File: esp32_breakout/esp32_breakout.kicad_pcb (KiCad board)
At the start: 2 copper layers, 48.3 x 70.4 mm, 16 parts, among them J10 UART1, J12 SPI1, J14 DAC1, J15 DAC2, J16 SPI2, U1 ESP32-DEVKITC-32D, X1 AUX1, X2 AUX2

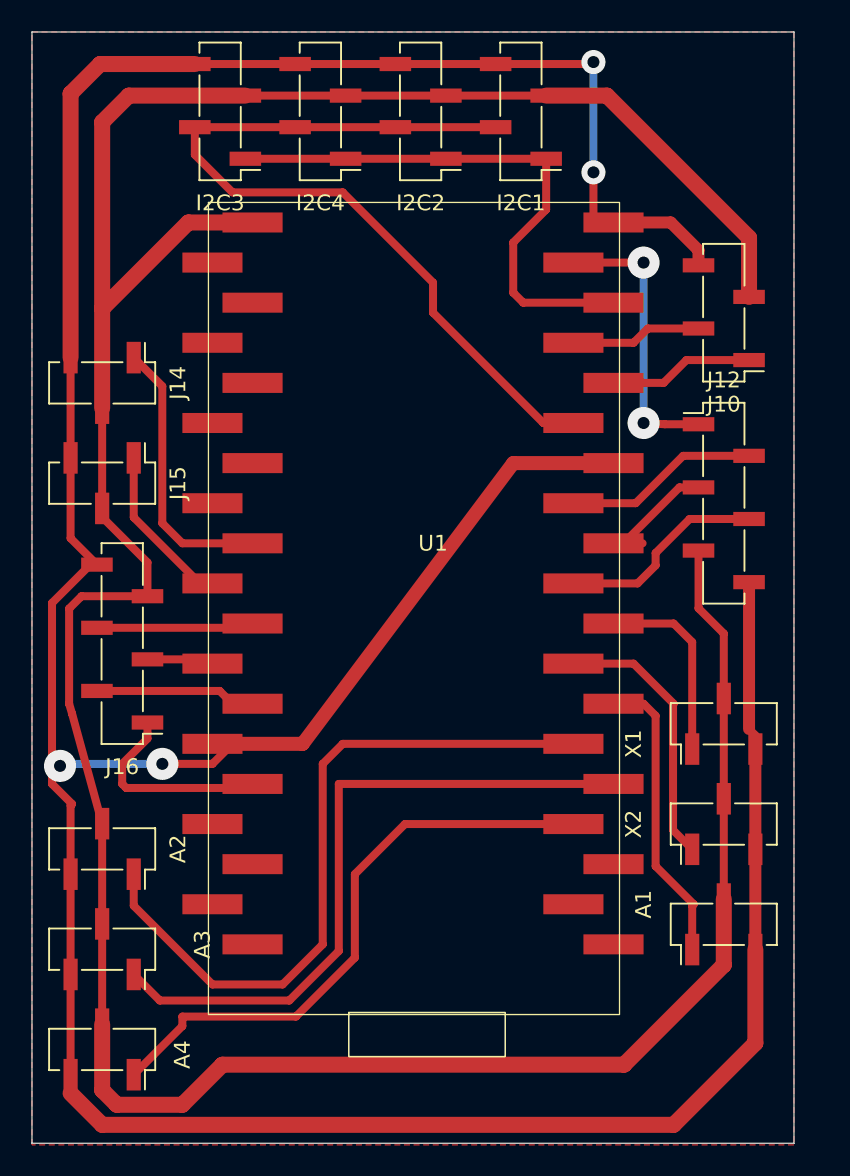
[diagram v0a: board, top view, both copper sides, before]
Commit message: little bigger board
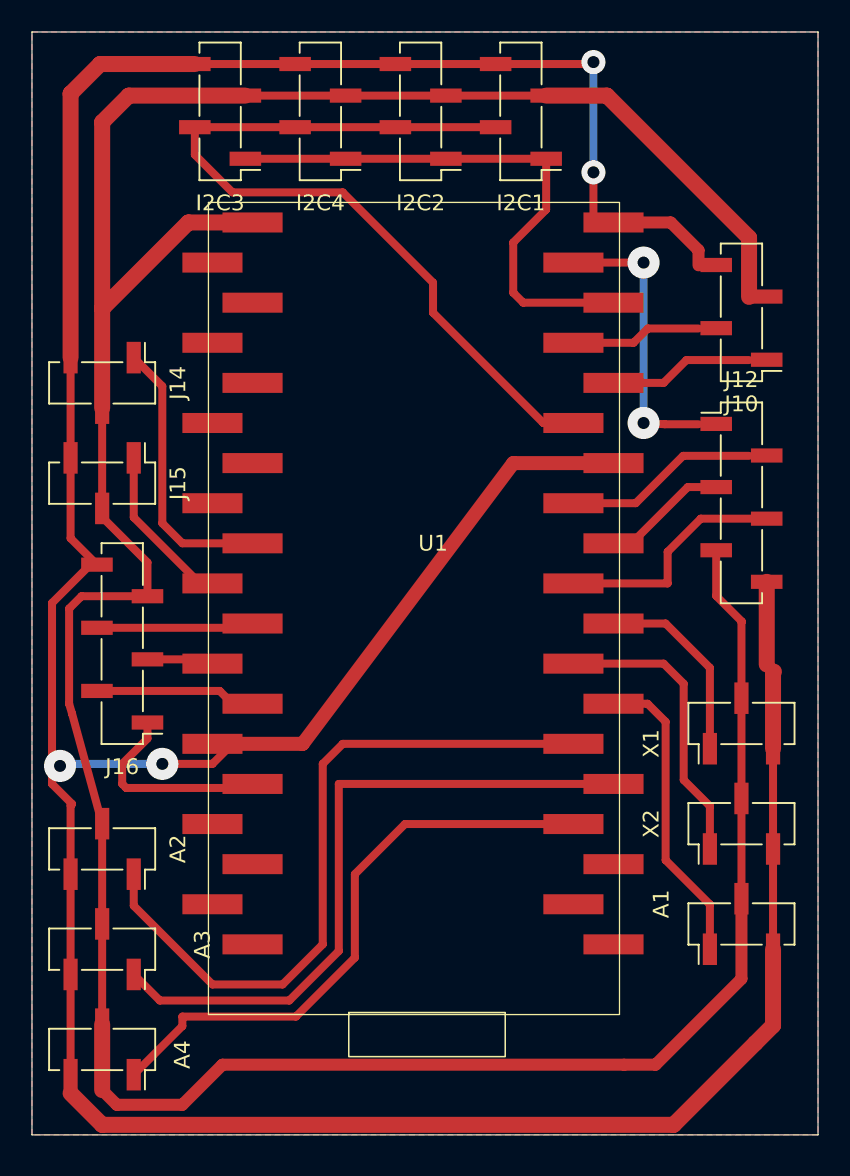
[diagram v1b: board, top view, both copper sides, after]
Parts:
- moved A1 1.12 mm to (44.9, 56.5)
- moved J10 1.12 mm to (44.9, 17.8)
- moved J12 1.12 mm to (44.9, 29.8)
- moved X1 1.12 mm to (44.9, 43.8)
- moved X2 1.12 mm to (44.9, 50.1)
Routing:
- net SPI_SCK: track 11.2 -> 9.25 mm
- net SPI_CS: track 12.0 -> 13.8 mm
- net 3V3: track 197.3 -> 198.9 mm
- net SIG2: track 15.9 -> 17.4 mm
- net GND: track 237.2 -> 237.7 mm
- net ADC1: track 20.1 -> 20.6 mm
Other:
- board size 48.3 x 70.4 mm -> 49.8 x 69.8 mm
